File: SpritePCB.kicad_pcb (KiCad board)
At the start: 2 copper layers, 54 x 50.5 mm, 11 parts, among them J1 Ribbon_Conn, J2 Extruder, J3 CRtouch, J4 FAN2, J5 Thermistor, J6 Heater, J7 FAN1

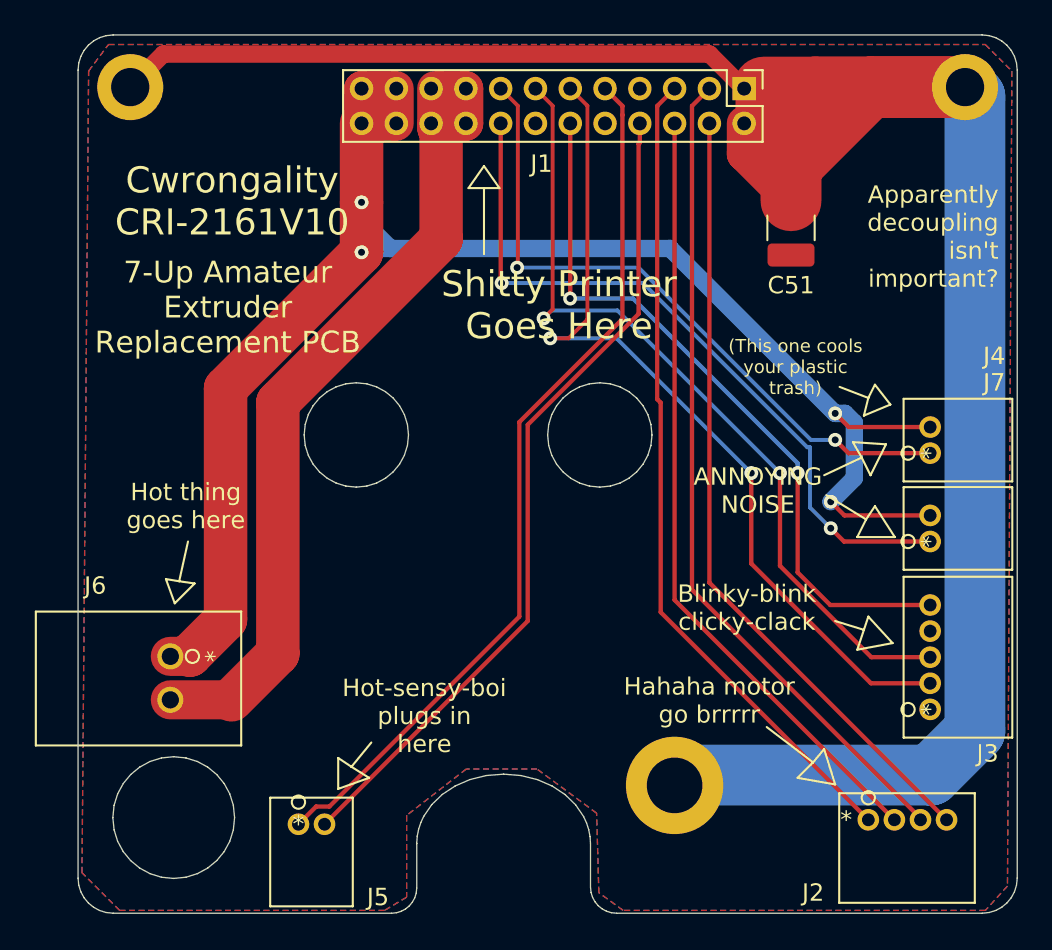
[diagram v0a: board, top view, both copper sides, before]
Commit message: Corrected misaligned drills
Corrected misaligned motor mount hole (originally slightly too high and too far left); shifted FFC connector left slightly to align better with the cable bracket; widened cutout for POM adjuster slightly on the left; enlarged M2 mounting holes for cable bracket slightly. 

After receiving the first batch of boards, I noticed that I'd done math wrong on the motor mounting hole positions. (Did the math based on the edge, not the centre, because I'm stupid. I also made some slight tweaks to other items to get it to line up a little better with the original board's cutouts, but all in, it was actually pretty close!

One thing to note: The connectors that were previously SMD ZH connectors were in places where the mount for the sprite was totally flat, so you'll likely need to snip the legs down _very_ flush once the through-hole connectors are mounted. The single through-hole XH on the original board has a cutout in the mount behind it; you might consider filing out a similar groove behind the new through-holes in the other side.
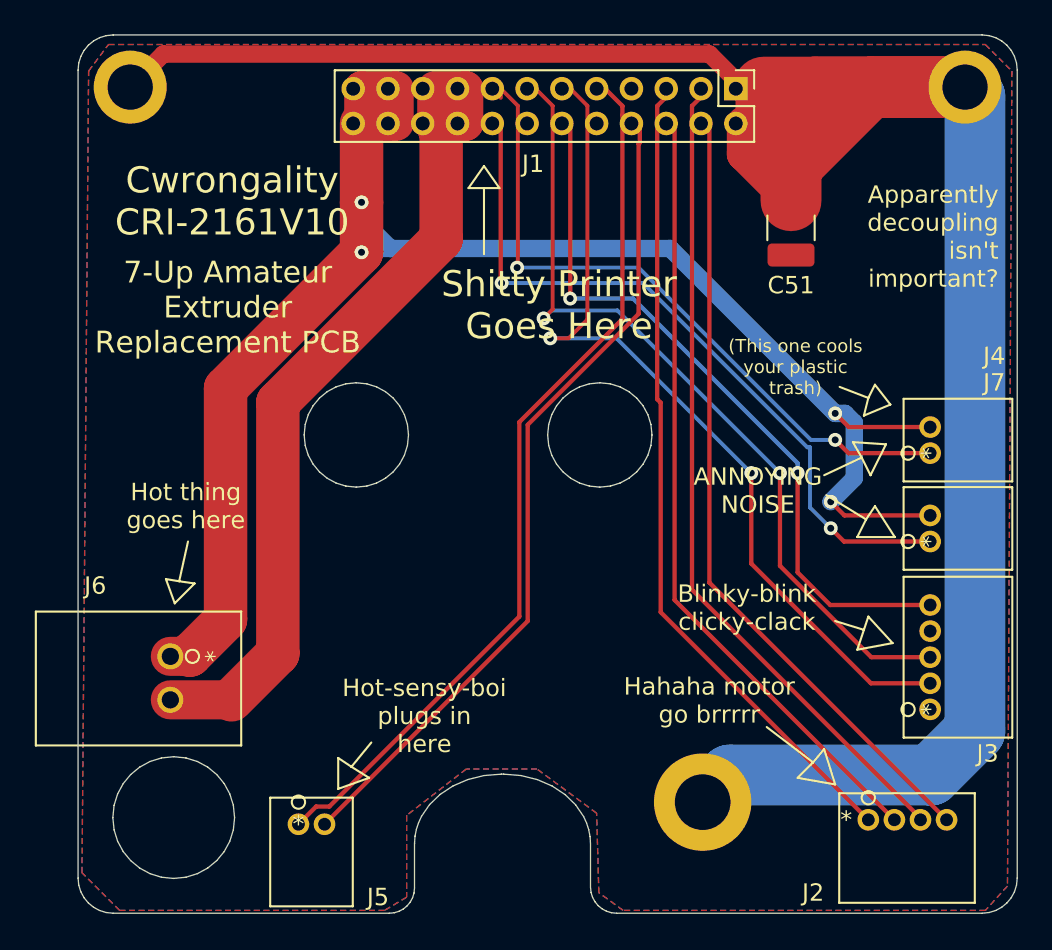
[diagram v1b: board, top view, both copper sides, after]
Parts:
- moved H3 1.88 mm to (65.9, 83.6)
- moved J1 0.48 mm to (67.8, 42.5)
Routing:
- net /MNT_HOLE: track 137.7 -> 136.5 mm
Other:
- outline, holes or cut-outs redrawn
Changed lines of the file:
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@@
   (general
     (thickness 1.6)
-    (drawings 227)
+    (drawings 228)
     (tracks 140)
     (zones 0)
@@
   (layers
     (0 F.Cu signal hide)
-    (31 B.Cu signal hide)
+    (31 B.Cu signal)
     (32 B.Adhes user)
     (33 F.Adhes user)
@@
   )
   (setup
-    (last_trace_width 0.25)
+    (last_trace_width 3.5)
     (user_trace_width 0.225)
     (user_trace_width 1)
@@
     (mod_text_size 1 1)
     (mod_text_width 0.15)
-    (pad_size 1.35 1.35)
-    (pad_drill 0.8)
+    (pad_size 4.2 4.2)
+    (pad_drill 2.6)
     (pad_to_mask_clearance 0)
     (aux_axis_origin 0 0)
     (visible_elements 7FFFFFFF)
     (pcbplotparams
-      (layerselection 0x010fc_ffffffff)
+      (layerselection 0x010ff_ffffffff)
       (usegerberextensions false)
       (usegerberattributes true)
@@
   )
   (module Connector_PinHeader_2.00mm:PinHeader_2x12_P2.00mm_Vertical (layer F.Cu)
-    (at 68.3 42.539 270)
+    (at 67.818 42.545 270)
     (descr "Through hole straight pin header, 2x12, 2.00mm pitch, double rows")
     (tags "Through hole pin header THT 2x12 2.00mm double row")
@@
   )
   (module MountingHole:MountingHole_3.2mm_M3_DIN965_Pad (layer F.Cu)
-    (at 64.3 82.603886)
+    (at 65.913 83.566)
     (descr "Mounting Hole 3.2mm, M3, DIN965")
     (tags "mounting hole 3.2mm m3 din965")
@@
       (effects (font (size 1 1) (thickness 0.15)))
     )
-    (pad 1 thru_hole circle (at 0 0) (size 3.8 3.8) (drill 2.2) (layers *.Cu *.Mask)
+    (pad 1 thru_hole circle (at 0 0) (size 4.2 4.2) (drill 2.6) (layers *.Cu *.Mask)
       (net 1 /MNT_HOLE))
   )
@@
       (effects (font (size 1 1) (thickness 0.15)))
     )
-    (pad 1 thru_hole circle (at 0 0) (size 3.8 3.8) (drill 2.2) (layers *.Cu *.Mask)
+    (pad 1 thru_hole circle (at 0 0) (size 4.2 4.2) (drill 2.6) (layers *.Cu *.Mask)
       (net 1 /MNT_HOLE))
   )
@@
       (effects (font (size 0.8 0.8) (thickness 0.12)))
     )
-    (pad 2 smd roundrect (at 1.5625 0 270) (size 1.325 2.7) (layers F.Cu F.Paste F.Mask) (roundrect_rratio 0.1886784905660377)
+    (pad 2 smd roundrect (at 1.5625 0 270) (size 1.325 2.7) (layers F.Cu F.Paste F.Mask) (roundrect_rratio 0.1886777358490566)
       (net 15 /MNT_HOLE_F))
-    (pad 1 smd roundrect (at -1.5625 0 270) (size 1.325 2.7) (layers F.Cu F.Paste F.Mask) (roundrect_rratio 0.1886784905660377)
+    (pad 1 smd roundrect (at -1.5625 0 270) (size 1.325 2.7) (layers F.Cu F.Paste F.Mask) (roundrect_rratio 0.1886777358490566)
       (net 1 /MNT_HOLE))
   )
+  (gr_line (start 54.46866 81.95652) (end 54.34166 81.95652) (layer Edge.Cuts) (width 0.018))
   (gr_line (start 75.184 61.341) (end 75.438 60.325) (layer F.SilkS) (width 0.12))
   (gr_line (start 76.708 60.706) (end 75.184 61.341) (layer F.SilkS) (width 0.12))
@@
   (gr_line (start 36.205008 81.024993) (end 36.86181 81.22907) (layer Edge.Cuts) (width 0.018))
   (gr_line (start 35.50002 80.95383) (end 36.205008 81.024993) (layer Edge.Cuts) (width 0.018))
-  (gr_line (start 49.47333 88.502784) (end 49.47333 88.502784) (layer Edge.Cuts) (width 0.018))
-  (gr_line (start 49.47333 85.95516) (end 49.47333 88.502784) (layer Edge.Cuts) (width 0.018))
-  (gr_line (start 49.473389 85.92933) (end 49.47333 85.95516) (layer Edge.Cuts) (width 0.018))
-  (gr_line (start 49.50218 85.522992) (end 49.473389 85.92933) (layer Edge.Cuts) (width 0.018))
-  (gr_line (start 49.580378 85.128423) (end 49.50218 85.522992) (layer Edge.Cuts) (width 0.018))
-  (gr_line (start 49.705493 84.747619) (end 49.580378 85.128423) (layer Edge.Cuts) (width 0.018))
-  (gr_line (start 49.875035 84.382571) (end 49.705493 84.747619) (layer Edge.Cuts) (width 0.018))
-  (gr_line (start 50.337446 83.707717) (end 49.875035 84.382571) (layer Edge.Cuts) (width 0.018))
-  (gr_line (start 50.947691 83.119807) (end 50.337446 83.707717) (layer Edge.Cuts) (width 0.018))
-  (gr_line (start 51.685852 82.634787) (end 50.947691 83.119807) (layer Edge.Cuts) (width 0.018))
-  (gr_line (start 52.532013 82.268602) (end 51.685852 82.634787) (layer Edge.Cuts) (width 0.018))
-  (gr_line (start 53.466254 82.037198) (end 52.532013 82.268602) (layer Edge.Cuts) (width 0.018))
-  (gr_line (start 54.46866 81.95652) (end 53.466254 82.037198) (layer Edge.Cuts) (width 0.018))
+  (gr_line (start 49.34633 88.502784) (end 49.34633 88.502784) (layer Edge.Cuts) (width 0.018))
+  (gr_line (start 49.34633 85.95516) (end 49.34633 88.502784) (layer Edge.Cuts) (width 0.018))
+  (gr_line (start 49.346389 85.92933) (end 49.34633 85.95516) (layer Edge.Cuts) (width 0.018))
+  (gr_line (start 49.37518 85.522992) (end 49.346389 85.92933) (layer Edge.Cuts) (width 0.018))
+  (gr_line (start 49.453378 85.128423) (end 49.37518 85.522992) (layer Edge.Cuts) (width 0.018))
+  (gr_line (start 49.578493 84.747619) (end 49.453378 85.128423) (layer Edge.Cuts) (width 0.018))
+  (gr_line (start 49.748035 84.382571) (end 49.578493 84.747619) (layer Edge.Cuts) (width 0.018))
+  (gr_line (start 50.210446 83.707717) (end 49.748035 84.382571) (layer Edge.Cuts) (width 0.018))
+  (gr_line (start 50.820691 83.119807) (end 50.210446 83.707717) (layer Edge.Cuts) (width 0.018))
+  (gr_line (start 51.558852 82.634787) (end 50.820691 83.119807) (layer Edge.Cuts) (width 0.018))
+  (gr_line (start 52.405013 82.268602) (end 51.558852 82.634787) (layer Edge.Cuts) (width 0.018))
+  (gr_line (start 53.339254 82.037198) (end 52.405013 82.268602) (layer Edge.Cuts) (width 0.018))
+  (gr_line (start 54.34166 81.95652) (end 53.339254 82.037198) (layer Edge.Cuts) (width 0.018))
   (gr_line (start 55.474863 82.037818) (end 54.46866 81.95652) (layer Edge.Cuts) (width 0.018))
   (gr_line (start 56.412289 82.270959) (end 55.474863 82.037818) (layer Edge.Cuts) (width 0.018))
@@
   (gr_line (start 31.613108 89.912814) (end 31.234046 89.795033) (layer Edge.Cuts) (width 0.018))
   (gr_line (start 32.019975 89.953886) (end 31.613108 89.912814) (layer Edge.Cuts) (width 0.018))
-  (gr_line (start 48.02229 89.953886) (end 32.019975 89.953886) (layer Edge.Cuts) (width 0.018))
-  (gr_line (start 48.314726 89.924406) (end 48.02229 89.953886) (layer Edge.Cuts) (width 0.018))
-  (gr_line (start 48.587101 89.839856) (end 48.314726 89.924406) (layer Edge.Cuts) (width 0.018))
-  (gr_line (start 48.833581 89.706069) (end 48.587101 89.839856) (layer Edge.Cuts) (width 0.018))
-  (gr_line (start 49.048331 89.528881) (end 48.833581 89.706069) (layer Edge.Cuts) (width 0.018))
-  (gr_line (start 49.225515 89.314124) (end 49.048331 89.528881) (layer Edge.Cuts) (width 0.018))
-  (gr_line (start 49.3593 89.067633) (end 49.225515 89.314124) (layer Edge.Cuts) (width 0.018))
-  (gr_line (start 49.44385 88.795241) (end 49.3593 89.067633) (layer Edge.Cuts) (width 0.018))
-  (gr_line (start 49.47333 88.502784) (end 49.44385 88.795241) (layer Edge.Cuts) (width 0.018))
+  (gr_line (start 47.89529 89.953886) (end 32.019975 89.953886) (layer Edge.Cuts) (width 0.018))
+  (gr_line (start 48.187726 89.924406) (end 47.89529 89.953886) (layer Edge.Cuts) (width 0.018))
+  (gr_line (start 48.460101 89.839856) (end 48.187726 89.924406) (layer Edge.Cuts) (width 0.018))
+  (gr_line (start 48.706581 89.706069) (end 48.460101 89.839856) (layer Edge.Cuts) (width 0.018))
+  (gr_line (start 48.921331 89.528881) (end 48.706581 89.706069) (layer Edge.Cuts) (width 0.018))
+  (gr_line (start 49.098515 89.314124) (end 48.921331 89.528881) (layer Edge.Cuts) (width 0.018))
+  (gr_line (start 49.2323 89.067633) (end 49.098515 89.314124) (layer Edge.Cuts) (width 0.018))
+  (gr_line (start 49.31685 88.795241) (end 49.2323 89.067633) (layer Edge.Cuts) (width 0.018))
+  (gr_line (start 49.34633 88.502784) (end 49.31685 88.795241) (layer Edge.Cuts) (width 0.018))
   (gr_text "If you're reading this,\nyou fucked up." (at 55.626 70.612) (layer B.SilkS)
     (effects (font (size 2 2) (thickness 0.4)) (justify mirror))
@@
   (segment (start 81 42.4539) (end 72.3541 42.4539) (width 3.5) (layer F.Cu) (net 1))
   (segment (start 72.3541 42.4539) (end 69.977 44.831) (width 3.5) (layer F.Cu) (net 1))
-  (segment (start 64.894187 82.009699) (end 64.3 82.603886) (width 3.5) (layer B.Cu) (net 1))
-  (segment (start 79.023307 82.009699) (end 64.894187 82.009699) (width 3.5) (layer B.Cu) (net 1))
   (segment (start 81.566301 79.466705) (end 79.023307 82.009699) (width 3.5) (layer B.Cu) (net 1))
   (segment (start 81.566301 43.020201) (end 81.566301 79.466705) (width 3.5) (layer B.Cu) (net 1))
   (segment (start 81 42.4539) (end 81.566301 43.020201) (width 3.5) (layer B.Cu) (net 1))
+  (segment (start 67.469301 82.009699) (end 65.913 83.566) (width 3.5) (layer B.Cu) (net 1))
+  (segment (start 79.023307 82.009699) (end 67.469301 82.009699) (width 3.5) (layer B.Cu) (net 1))
   (segment (start 46.3 42.539) (end 48.174999 42.539) (width 2) (layer F.Cu) (net 2))
   (segment (start 46.3 42.539) (end 46.3 44.539) (width 2) (layer F.Cu) (net 2))

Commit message: Fix issue #1: overlapping tracks/signals introduced in commit 18d3b11
Moving the dual-row header in commit 18d3b1 resulted in misaligned traces overlapping with the new hole positions. Don't commit changes while tired, folks.
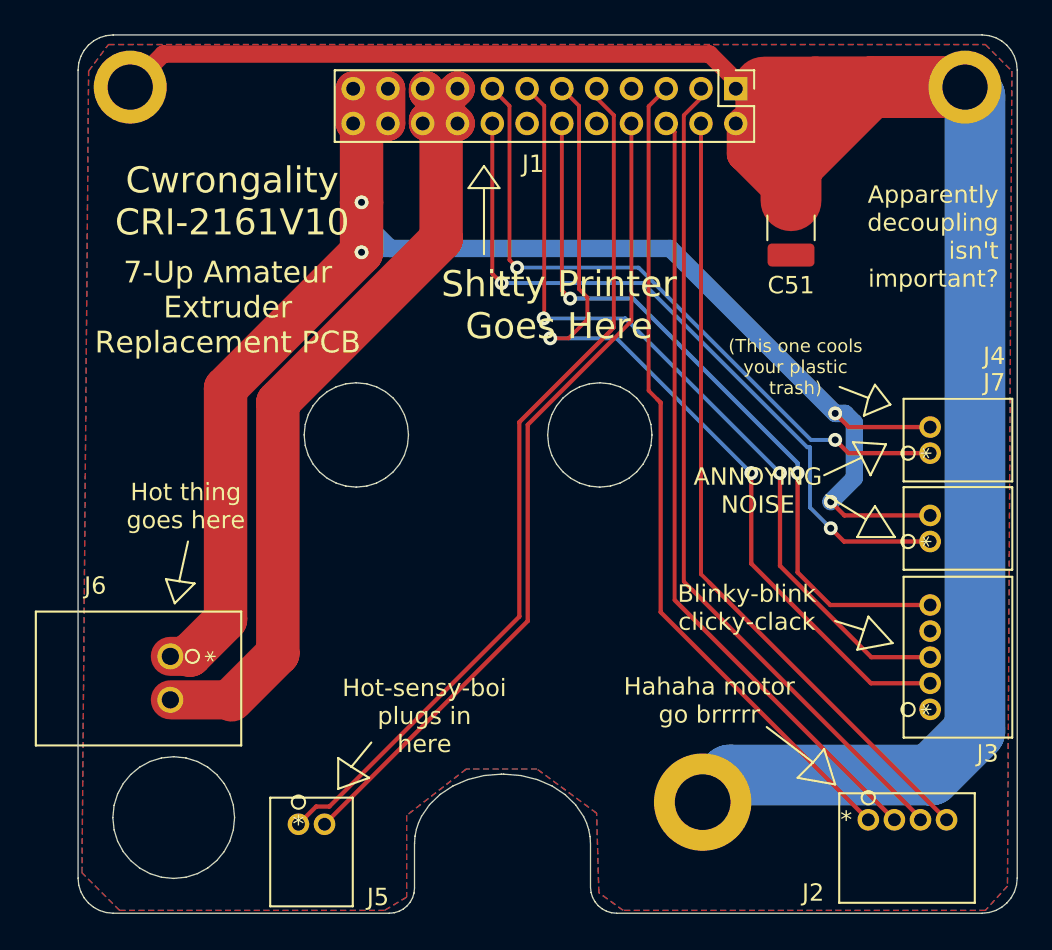
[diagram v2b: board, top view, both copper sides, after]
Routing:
- net /HEATER_2: track 49.0 -> 52.6 mm
- net /HEATER_FAN_COM: track 99.3 -> 101.3 mm
- net /CRTOUCH_3: track 47.6 -> 47.1 mm
